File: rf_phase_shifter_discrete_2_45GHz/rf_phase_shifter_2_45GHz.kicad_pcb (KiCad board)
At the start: 2 copper layers, 43.1 x 21 mm, 16 parts, among them J1 CON-SMA-EDGE-S, J2 CON-SMA-EDGE-S, J3 CON-SMA-EDGE-S

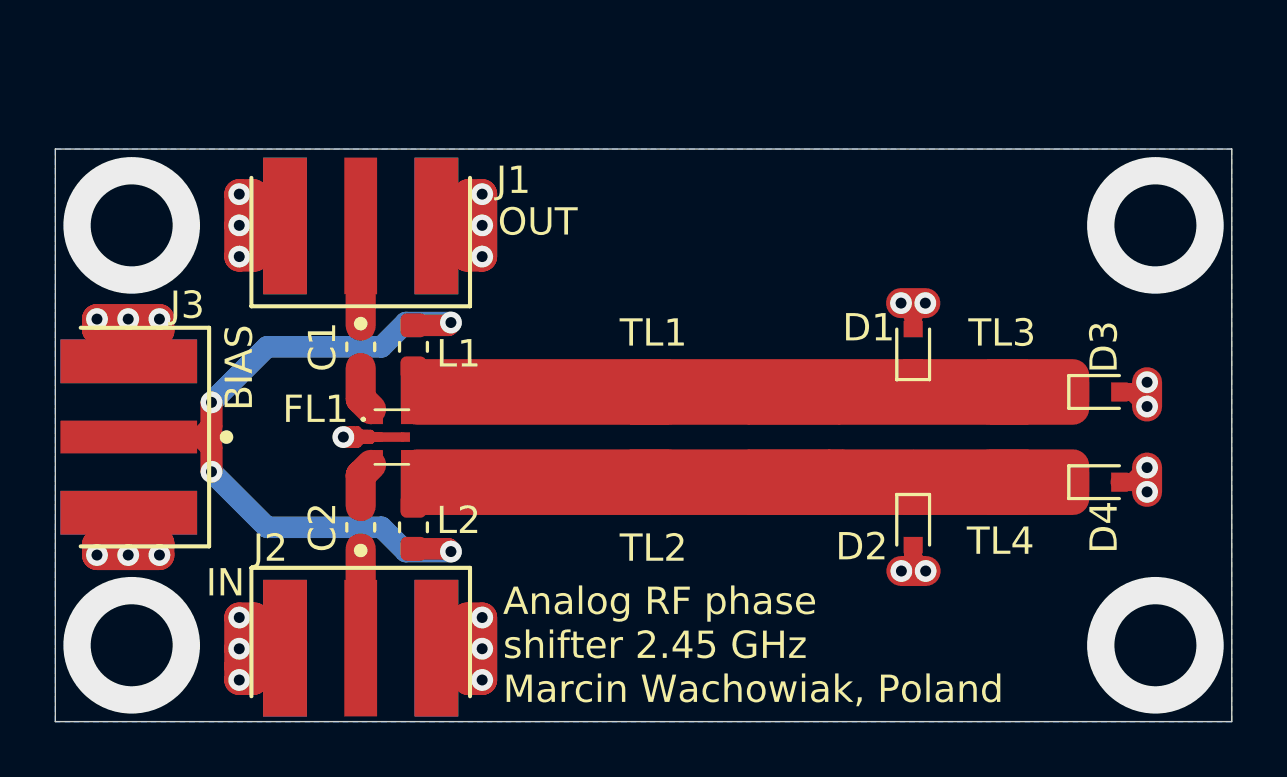
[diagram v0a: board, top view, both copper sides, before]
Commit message: Designed pcb for discrete component version, generated gerbers and updated docs
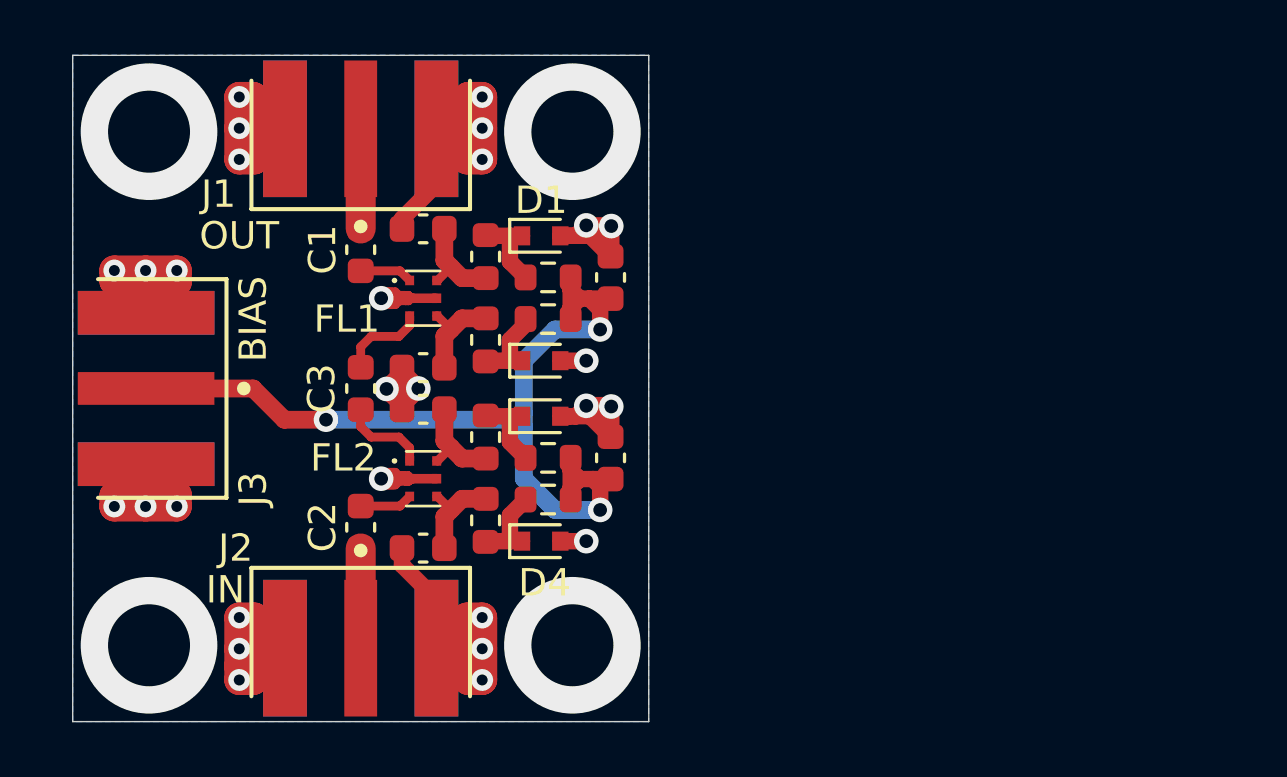
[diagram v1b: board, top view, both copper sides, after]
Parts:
- removed TL1, TL2: TL_13_2_45GHz, analog_rf_phase_shifter_module:TL_13_2_45GHz
- removed TL3, TL4: TL_24_2_45GHz, analog_rf_phase_shifter_module:TL_24_2_45GHz
- added C3: 100p, Capacitor_SMD:C_0603_1608Metric, F.Cu at (84.5, 57.1)
- added C4: 2p, Capacitor_SMD:C_0603_1608Metric, F.Cu at (86.7, 51.3)
- added C5: 2p, Capacitor_SMD:C_0603_1608Metric, F.Cu at (86.7, 56.4)
- added C6: 2p, Capacitor_SMD:C_0603_1608Metric, F.Cu at (86.7, 57.9)
- added C7: 2p, Capacitor_SMD:C_0603_1608Metric, F.Cu at (86.7, 63.0)
- added C8: 100p, Capacitor_SMD:C_0603_1608Metric, F.Cu at (93.6, 53.1)
- added C9: 100p, Capacitor_SMD:C_0603_1608Metric, F.Cu at (93.6, 59.7)
- added FL2: C2327J5003AHF, analog_rf_phase_shifter_module:C2327J5003AHF, F.Cu at (86.7, 60.5)
- added L3: 1.8n, Inductor_SMD:L_0603_1608Metric, F.Cu at (89.0, 58.9)
- added L4: 1.8n, Inductor_SMD:L_0603_1608Metric, F.Cu at (89.0, 62.0)
- added R1: 200, Resistor_SMD:R_0603_1608Metric, F.Cu at (91.3, 53.1)
- added R2: 200, Resistor_SMD:R_0603_1608Metric, F.Cu at (91.3, 54.6)
- added R3: 200, Resistor_SMD:R_0603_1608Metric, F.Cu at (91.3, 59.7)
- added R4: 200, Resistor_SMD:R_0603_1608Metric, F.Cu at (91.3, 61.2)
- C1, C2: value 100pF -> 100p
- L1, L2: value 220n -> 1.8n
- moved D4 20.6 mm to (91.1, 62.7)
- moved D3 20.5 mm to (91.1, 58.2)
- moved D2 14.9 mm to (91.1, 56.1), turned to 0 degrees
- moved D1 14.2 mm to (91.1, 51.6), turned to 0 degrees
- moved L2 7.35 mm to (89.0, 55.4), turned to -90 degrees
- moved FL1 5.21 mm to (86.7, 53.8)
- moved L1 4.23 mm to (89.0, 52.3), turned to 90 degrees
- moved C1 3.56 mm to (84.5, 52.1)
- moved J1 3.56 mm to (84.5, 40.4)
- moved J3 1.89 mm to (69.3, 57.1)
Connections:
- FL1 pad 3: Net-(C2-Pad2) -> Net-(C3-Pad2)
- FL1 pad 4: Net-(FL1-Pad4) -> Net-(C5-Pad1)
- FL1 pad 6: Net-(FL1-Pad6) -> Net-(C4-Pad1)
- J3 pad 1: Net-(J3-Pad1) -> Net-(C8-Pad1)
- L1 pad 1: Net-(J3-Pad1) -> Net-(C4-Pad1)
- L1 pad 2: Net-(FL1-Pad6) -> Net-(D1-Pad1)
- L2 pad 1: Net-(J3-Pad1) -> Net-(C5-Pad1)
- L2 pad 2: Net-(FL1-Pad4) -> Net-(D2-Pad1)
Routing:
- net Net-(C8-Pad1): track 0.00 -> 36.2 mm, vias 0 -> 3
- net Net-(D2-Pad1): track 36.2 -> 3.14 mm
- net Net-(J3-Pad1): track 30.7 -> 0.00 mm, vias 4 -> 0
- net GND: track 70.1 -> 94.5 mm, vias 31 -> 32
- net Net-(D1-Pad1): track 16.8 -> 3.10 mm
- net Net-(FL1-Pad4): track 9.93 -> 0.00 mm
- net Net-(FL1-Pad6): track 6.22 -> 0.00 mm
- net Net-(C5-Pad1): track 0.00 -> 3.66 mm
- net Net-(C4-Pad1): track 0.00 -> 3.66 mm
- net Net-(C7-Pad1): track 0.00 -> 3.66 mm
- net Net-(C6-Pad1): track 0.00 -> 3.66 mm
- net Net-(C3-Pad2): track 0.00 -> 3.21 mm
- net Net-(C3-Pad1): track 0.00 -> 3.21 mm
- net Net-(D4-Pad1): track 0.00 -> 3.10 mm
- net Net-(L3-Pad2): track 0.00 -> 3.10 mm
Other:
- board size 43.1 x 21 mm -> 21.1 x 24.4 mm
- net class Default removed
